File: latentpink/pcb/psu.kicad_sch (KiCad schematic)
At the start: 0 parts

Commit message: Continued initial schematic capture and floorplanning
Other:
- company: (none) -> Antikernel Labs
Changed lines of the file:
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@@
 (kicad_sch (version 20211123) (generator eeschema)
   (paper "A4")
+  (title_block
+    (date "2023-04-22")
+    (rev "0.1")
+    (company "Antikernel Labs")
+    (comment 1 "Andrew D. Zonenberg")
+  )
 )

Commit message: Continued initial schematic capture
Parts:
- added C100, C101, C102, C103, C104, C105, C89, C90, C94, C95: 22 uF 25V, symbol device:C
- added C106: 4.7 uF, azonenberg_pcb:EIA_0603_CAP_NOSILK, symbol device:C
- added C107, C108, C109, C112, C113, C114, C91, C92, C93, C96, C97: 220 uF, symbol device:C
- added C110, C115, C116, C119, C123: 0.47 uF, azonenberg_pcb:EIA_0402_CAP_NOSILK, symbol device:C
- added C111: 0.1 uF, azonenberg_pcb:EIA_0402_CAP_NOSILK, symbol device:C
- added C117, C122: EEH-ZS1E102UV, symbol device:CP1
- added C118, C120: DNP, symbol device:CP1
- added C121: 0.015 uF, azonenberg_pcb:EIA_0603_CAP_NOSILK, symbol device:C
- added D1, D2, D3: GREEN, azonenberg_pcb:EIA_0603_LED, symbol device:LED
- added D4: RED, azonenberg_pcb:EIA_0603_LED, symbol device:LED
- added F1: 4A, symbol power-azonenberg:FUSE_PWROUT_2
- added FB1: TBD, symbol passive-azonenberg:FERRITE_SMALL2
- added J13: CONN_01X05, azonenberg_pcb:CONN_HEADER_2.54MM_1x5, symbol conn:CONN_01X05
- added J14: CONN_01X03, azonenberg_pcb:CONN_HEADER_2.54MM_1x3, symbol conn:CONN_01X03
- added J6: BARREL_JACK, azonenberg_pcb:CONN_CUI_PJ-058BH_HIPWR_BARREL_NOSLOT, symbol power-azonenberg:BARREL_JACK
- added R1: 16K, symbol device:R
- added R10: 4.7k, azonenberg_pcb:EIA_0402_RES_NOSILK, symbol device:R
- added R11: 160, symbol device:R
- added R12: 22, symbol device:R
- added R13: 300, symbol device:R
- added R14, R16, R18, R20, R22, R5, R7: 10K, azonenberg_pcb:EIA_0402_RES_NOSILK, symbol device:R
- added R15, R17, R19, R21, R23, R29, R31: 1K, azonenberg_pcb:EIA_0402_RES_NOSILK, symbol device:R
- added R2, R6: 0, azonenberg_pcb:EIA_0402_RES_NOSILK, symbol device:R
- added R24, R25, R26, R27: 470, azonenberg_pcb:EIA_0402_RES_NOSILK, symbol device:R
- added R28: 470 1/4W, symbol device:R
- added R8: 3k, symbol device:R
- added R9: 2.2k, symbol device:R
- added TP1, TP2, TP3, TP4, TP5: TESTPOINT, azonenberg_pcb:TESTPOINT_SMT_0.5MM, symbol conn:CONN_01X01
- added U10: MYMGK1R812ERSR, azonenberg_pcb:MODULE_MURATA_MYMGK1R812, symbol power-azonenberg:MYMGK1R812ERSR
- added U11, U13, U14, U15: MYMGK00504ERSR, azonenberg_pcb:MODULE_MURATA_MYMGK00504ERSR, symbol power-azonenberg:MYMGK00504ERSR
- added U12: STM32L031-QFN32, azonenberg_pcb:QFN_32_0.5MM_5x5MM, symbol st-azonenberg:STM32L031-QFN32
- added U16, U17: NCP45521IMNTWG-H, azonenberg_pcb:DFN_8_0.5MM_2x2MM, symbol power-azonenberg:NCP45525
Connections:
- new net: D3.2 (A), R26.2
- new net: C121.1, U16.6 (SR)
- new net: R10.2, R13.2
- new net: R8.1, U13.4 (TRIM)
- new net: R11.2, R8.2
- new net: D4.2 (A), R27.2
- new net: R5.2, R6.2
- new net: R9.1, U14.4 (TRIM)
- new net: R12.2, R9.2
- new net: R10.1, U15.4 (TRIM)
- new net: R1.2, R2.2
- new net: R5.1, U11.4 (TRIM)
- new net: R1.1, U10.22 (TRIM)
- new net: D1.2 (A), R24.2
- new net: F1.2, FB1.1
- new net: D2.2 (A), R25.2
- new net 12V0: C100.1, C101.1, C102.1, C103.1, C104.1, C105.1, C117.1, C118.1, C120.1, C122.1, C89.1, C90.1, C94.1, C95.1, R28.2, U10.1 (VIN), U10.2 (VIN), U10.3 (VIN), U10.4 (VIN), U10.5 (VIN), U10.6 (VIN), U11.1 (VIN), U11.2 (VIN), U13.1 (VIN), U13.2 (VIN), U14.1 (VIN), U14.2 (VIN), U15.1 (VIN), U15.2 (VIN), U16.7 (VOUT), U16.8 (VOUT)
- new net 12V0_BLEED: R28.1, U16.5 (BLEED)
- new net 12V0_EN: R29.1, U12.22 (PA12), U16.2 (EN)
- new net 12V0_FUSED: FB1.2, U16.1 (VIN), U16.PAD (VIN)
- new net 12V0_RAW: F1.1, J6.1 (PWR)
- new net 1V0: C91.1, C92.1, C93.1, U10.15 (VOUT), U10.16 (VOUT), U10.17 (VOUT), U10.18 (VOUT), U10.19 (VOUT), U10.20 (VOUT), U10.21 (SENSE)
- new net 1V0_EN: R15.1, U10.8 (EN), U12.19 (PA9)
- new net 1V0_PGOOD: R14.1, TP2.1 (P1), U10.7 (PGOOD), U12.6 (PA0)
- new net 1V2: C96.1, C97.1, U11.5 (SENSE), U11.6 (VOUT), U11.7 (VOUT)
- new net 1V2_EN: R17.1, U11.12 (ON/OFF), U12.18 (PA8)
- new net 1V2_PGOOD: R16.1, TP1.1 (P1), U11.11 (PGOOD), U12.7 (PA1)
- new net 1V8: C109.1, C114.1, U15.5 (SENSE), U15.6 (VOUT), U15.7 (VOUT), U17.1 (VIN), U17.PAD (VIN)
- new net 1V8_EN: R19.1, U12.13 (PA7), U15.12 (ON/OFF)
- new net 1V8_IO: U17.5 (BLEED), U17.7 (VOUT), U17.8 (VOUT)
- new net 1V8_IO_EN: R31.1, U12.25 (PA15), U17.2 (EN)
- new net 1V8_PGOOD: R18.1, TP5.1 (P1), U12.8 (PA2), U15.11 (PGOOD)
- new net 2V5: C107.1, C112.1, U13.5 (SENSE), U13.6 (VOUT), U13.7 (VOUT)
- new net 2V5_EN: R21.1, U12.12 (PA6), U13.12 (ON/OFF)
- new net 2V5_PGOOD: R20.1, TP3.1 (P1), U12.9 (PA3), U13.11 (PGOOD)
- new net 3V3: C108.1, C113.1, U14.5 (SENSE), U14.6 (VOUT), U14.7 (VOUT)
- new net 3V3_EN: R23.1, U12.11 (PA5), U14.12 (ON/OFF)
- new net 3V3_PGOOD: R22.1, TP4.1 (P1), U12.10 (PA4), U14.11 (PGOOD)
- new net 3V3_SB: C106.1, C110.1, C115.1, C116.1, C119.1, C123.1, J13.1 (P1), R14.2, R16.2, R18.2, R20.2, R22.2, R25.1, U12.1 (VDD), U12.17 (VDD), U12.5 (VDDA), U16.3 (VCC), U17.3 (VCC)
- new net ALL_OK: R24.1, U12.32 (PB8)
- new net FPGA_DONE: U12.16 (PB2)
- new net FPGA_INIT: U12.26 (PB3)
- new net FPGA_RST_N: U12.15 (PB1)
- new net GND: C100.2, C101.2, C102.2, C103.2, C104.2, C105.2, C106.2, C107.2, C108.2, C109.2, C110.2, C111.2, C112.2, C113.2, C114.2, C115.2, C116.2, C117.2, C118.2, C119.2, C120.2, C121.2, C122.2, C123.2, C89.2, C90.2, C91.2, C92.2, C93.2, C94.2, C95.2, C96.2, C97.2, D1.1 (K), D2.1 (K), D3.1 (K), D4.1 (K), J13.2 (P2), J14.3 (P3), J6.2 (GND), R11.1, R12.1, R13.1, R15.2, R17.2, R19.2, R2.1, R21.2, R23.2, R29.2, R31.2, R6.1, R7.2, U10.10 (GND), U10.11 (GND), U10.12 (GND), U10.13 (GND), U10.14 (GND), U10.23 (GND), U10.24 (GND), U10.25 (GND), U10.26 (GND), U10.27 (GND), U10.28 (GND), U10.29 (GND), U10.30 (GND), U10.31 (GND), U10.32 (GND), U10.33 (GND), U10.34 (GND), U10.35 (GND), U10.36 (GND), U10.37 (GND), U10.9 (GND), U11.10 (GND), U11.13 (GND), U11.14 (GND), U11.15 (GND), U11.16 (GND), U11.17 (GND), U11.18 (GND), U11.19 (GND), U11.20 (GND), U11.21 (GND), U11.22 (GND), U11.23 (GND), U11.3 (GND), U11.8 (GND), U11.9 (GND), U12.PAD (GND), U13.10 (GND), U13.13 (GND), U13.14 (GND), U13.15 (GND), U13.16 (GND), U13.17 (GND), U13.18 (GND), U13.19 (GND), U13.20 (GND), U13.21 (GND), U13.22 (GND), U13.23 (GND), U13.3 (GND), U13.8 (GND), U13.9 (GND), U14.10 (GND), U14.13 (GND), U14.14 (GND), U14.15 (GND), U14.16 (GND), U14.17 (GND), U14.18 (GND), U14.19 (GND), U14.20 (GND), U14.21 (GND), U14.22 (GND), U14.23 (GND), U14.3 (GND), U14.8 (GND), U14.9 (GND), U15.10 (GND), U15.13 (GND), U15.14 (GND), U15.15 (GND), U15.16 (GND), U15.17 (GND), U15.18 (GND), U15.19 (GND), U15.20 (GND), U15.21 (GND), U15.22 (GND), U15.23 (GND), U15.3 (GND), U15.8 (GND), U15.9 (GND), U16.4 (GND), U17.4 (GND)
- new net HARD_RESET_REQ: U12.28 (PB5)
- new net MCU_HEARTBEAT: U12.27 (PB4)
- new net MCU_RST_N: U12.14 (PB0)
- new net PWR_FAIL: R27.1, U12.21 (PA11)
- new net PWR_OK: R26.1, U12.20 (PA10)
- new net SUPER_BOOT0: R7.1, U12.31 (BOOT0)
- new net SUPER_RST_N: C111.1, J13.5 (P5), U12.4 (NRST)
- new net SUPER_SWCLK: J13.3 (P3), U12.24 (PA14)
- new net SUPER_SWDIO: J13.4 (P4), U12.23 (PA13)
- new net SUPER_UART_RX: J14.1 (P1), U12.30 (PB7)
- new net SUPER_UART_TX: J14.2 (P2), U12.29 (PB6)
- no-connect marks 0 -> 4
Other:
- note added: "1.5V Vih, 1.1V Vil Internal: 6.8k pulldown, 22k pullup So should float at ~2.8V if undriven Add external 1K pulldown, equivalent 871 ohms Need 1.72 mA drive current for 1.5V, 2.87 mA for 2.5V"
- note added: "1.8V Vih Internal: 33K pulldown, 100K pullup So should float at ~2.7V if undriven"
- note added: "115 ohm nominal internal bleed resistance Max 400 mW internal dissipation 470 will gives discharge current of 20.5 mA Resistor will dissipate ~200 mW, 48 mW in IC"
- note added: "Cmax = 7.8A / SR SR for 3.3V supply = 13.5 kV/s Max C with default slew is only 578 uF To support 3000 uF (allowing for extra C), we need slew of 2.6 kV/sec or less SR = 31 uA / Csr so Csr = 11.9 nF"
- note added: "Power rail sequencing requirements: * QDR: VDD before VDDQ, VDDQ before or simultaneous w/ Vref * FPGA: 1V0 -> 1V8 -> VCCO * FPGA: 1V0 -> 1V2 Overall sequence: * Vin * 3V3_SB * 12V0 * 1V0 * 1V2 / 1V8 simultaneous * 1V8_IO, 2V5, 3V3 simultaneous * FPGA reset * MCU reset"
- note added: "Total output C 400 - 3000 uF"
- note added: "Total output C 660 - 5000 uF"
- note added: "Trim: Precision metal film 1/10W +/- 0.5%"

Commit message: Continued work on schematic, mostly power supply and QDR
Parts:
- added C167, C168: 0.1 uF, azonenberg_pcb:EIA_0402_CAP_NOSILK, symbol device:C
- added C169: 22 uF, symbol device:C
- added C170, C172: 0.47 uF, azonenberg_pcb:EIA_0402_CAP_NOSILK, symbol device:C
- added C171: 220 uF, symbol device:C
- added C173, C174: 2.2 uF, symbol device:C
- added R32: 1K, azonenberg_pcb:EIA_0402_RES_NOSILK, symbol device:R
- added R33, R34, R35, R36, R37, R38: 0, azonenberg_pcb:EIA_0402_RES_NOSILK, symbol device:R
- added R39: R, symbol device:R
- added TP16: TESTPOINT, azonenberg_pcb:TESTPOINT_SMT_0.5MM, symbol conn:CONN_01X01
- added U18: LP2996AMRE, azonenberg_pcb:SOIC_8_3.9MM_EPAD, symbol power-azonenberg:LP2996A
- added U19: TPS7A2533DRVR, symbol power-azonenberg:TPS7A25
- F1: value 4A -> ERB-RD4R00X; footprint (none) -> azonenberg_pcb:EIA_0402_CAP_NOSILK
- FB1: value TBD -> BLM31KN271SN1L; footprint (none) -> azonenberg_pcb:EIA_1206_CAP_NOSILK
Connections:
- net 12V0_FUSED: now also C174.1, U19.4 (EN), U19.6 (IN)
- net 1V0: now also R33.2, R35.2; no longer C91.1, C92.1, C93.1, U10.15 (VOUT), U10.16 (VOUT), U10.17 (VOUT), U10.18 (VOUT), U10.19 (VOUT), U10.20 (VOUT), U10.21 (SENSE)
- net 1V2: now also R34.2; no longer C96.1, C97.1, U11.6 (VOUT), U11.7 (VOUT)
- net 1V8: now also C169.1, C170.1, R38.2, U18.5 (VDDQ), U18.7 (PVIN); no longer C109.1, C114.1, U15.6 (VOUT), U15.7 (VOUT)
- net 2V5: now also R36.2; no longer C107.1, C112.1, U13.6 (VOUT), U13.7 (VOUT)
- net 3V3: now also C172.1, R37.2, U18.6 (AVIN); no longer C108.1, C113.1, U14.6 (VOUT), U14.7 (VOUT)
- net 3V3_SB: now also C173.1, R39.2, U19.1 (OUT)
- net GND: now also C167.2, C168.2, C169.2, C170.2, C171.2, C172.2, C173.2, C174.2, R32.2, U18.1 (GND), U18.PAD (GND), U19.5 (GND), U19.PAD (GND)
- net VTT_EN: now reaches U12.2 (PC14)
- net VTT_EN: now also R32.1, U18.2 (~{SD})
- new net 1V0_RAW: C91.1, C92.1, C93.1, R33.1, U10.15 (VOUT), U10.16 (VOUT), U10.17 (VOUT), U10.18 (VOUT), U10.19 (VOUT), U10.20 (VOUT)
- new net 1V0_SENSE: R35.1, U10.21 (SENSE)
- new net 1V2_RAW: C96.1, C97.1, R34.1, U11.6 (VOUT), U11.7 (VOUT)
- new net 1V8_RAW: C109.1, C114.1, R38.1, U15.6 (VOUT), U15.7 (VOUT)
- new net 2V5_RAW: C107.1, C112.1, R36.1, U13.6 (VOUT), U13.7 (VOUT)
- new net 3V3_RAW: C108.1, C113.1, R37.1, U14.6 (VOUT), U14.7 (VOUT)
- new net 3V3_SB_PGOOD: R39.1, TP16.1 (P1), U19.3 (PG)
- new net QDR_VREF: C167.1, U18.4 (VREF)
- new net QDR_VTT: C168.1, C171.1, U18.3 (VSENSE), U18.8 (VTT)
- no-connect marks 4 -> 3
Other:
- note added: "Place C168 near U18 pin 3"
- note added: "Place C169 by U18 pin 7 Place C170 by U18 pin 5"
- note added: "Slew rate 2.1 kV/sec, so 5.7 ms ramp time Estimated 6.3A peak inrush"
- note added: "TODO: FPGA_RST_N / FPGA_DONE / FPGA_INIT are LVCMOS18 Do we need level shifting? We can do open drain on outputs So should only be an issue for DONE input"
- moved on the sheet: C119, C121, D1, D2, D3, D4, R14, R15, R16, R17, R18, R19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

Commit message: Continued work on QSGMII subsystem
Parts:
- R28: footprint (none) -> azonenberg_pcb:EIA_0603_RES_NOSILK
- U19: footprint (none) -> azonenberg_pcb:DFN_6_0.65MM_2x2MM
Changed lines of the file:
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@@
   (paper "A3")
   (title_block
-    (date "2023-05-10")
+    (date "2023-05-14")
     (rev "0.1")
     (company "Antikernel Labs")
@@
     (property "Reference" "U19" (id 0) (at 337.185 71.281 0))
     (property "Value" "TPS7A2533DRVR" (id 1) (at 337.185 73.8179 0))
-    (property "Footprint" "" (id 2) (at 331.47 83.82 0)
+    (property "Footprint" "azonenberg_pcb:DFN_6_0.65MM_2x2MM" (id 2) (at 331.47 83.82 0)
       (effects (font (size 1.27 1.27)) hide)
     )
@@
     (property "Reference" "R28" (id 0) (at 194.31 24.13 90))
     (property "Value" "470 1/4W" (id 1) (at 187.96 26.67 90))
-    (property "Footprint" "" (id 2) (at 187.96 25.908 90)
-      (effects (font (size 1.27 1.27)) hide)
-    )
+    (property "Footprint" "azonenberg_pcb:EIA_0603_RES_NOSILK" (id 2) (at 187.96 25.908 90)
+      (effects (font (size 1.27 1.27)) hide)
+    )

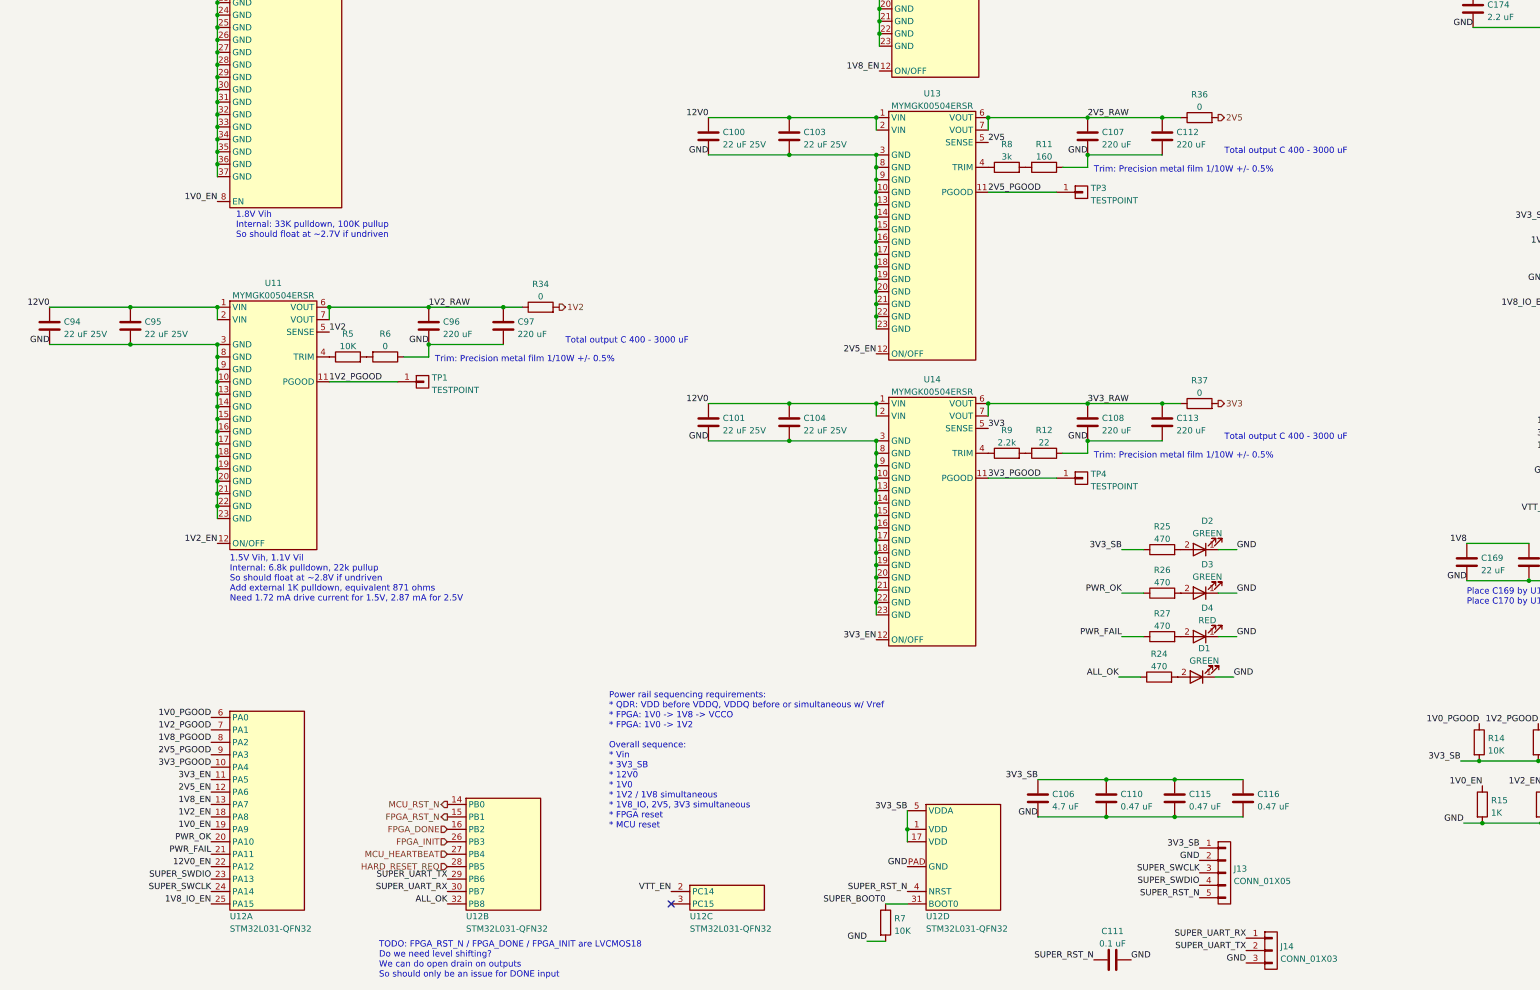
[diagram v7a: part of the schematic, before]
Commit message: Continued footprint assignment and miscellaneous missing tidbits of schematic
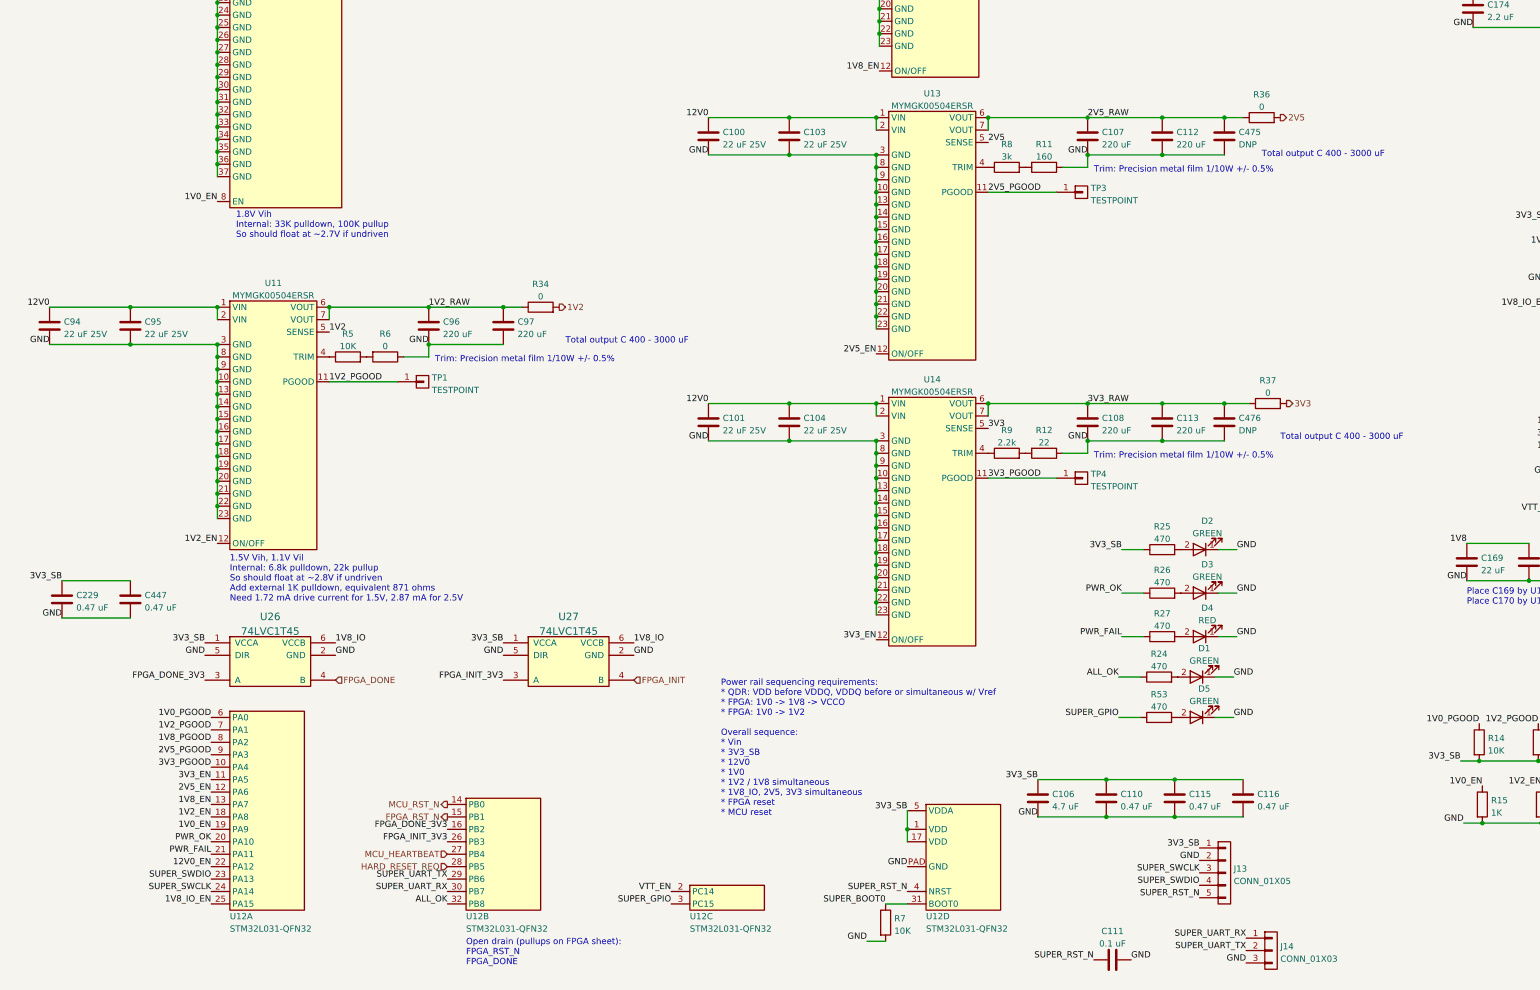
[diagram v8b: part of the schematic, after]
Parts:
- added C229, C447: 0.47 uF, azonenberg_pcb:EIA_0402_CAP_NOSILK, symbol device:C
- added C475, C476: DNP, azonenberg_pcb:EIA_1210_CAP_NOSILK, symbol device:C
- added D5: GREEN, azonenberg_pcb:EIA_0603_LED, symbol device:LED
- added R53: 470, azonenberg_pcb:EIA_0402_RES_NOSILK, symbol device:R
- added U26, U27: 74LVC1T45, azonenberg_pcb:DFN_6_0.5MM_1.45x1.00MM, symbol special-azonenberg:74LVC1T45
- C100, C101, C102, C103, C104, C105, C89, C90, C94, C95: footprint (none) -> azonenberg_pcb:EIA_1812_CAP_NOSILK
- C107, C108, C109, C112, C113, C114, C91, C92, C93, C96, C97: footprint (none) -> azonenberg_pcb:EIA_1210_CAP_NOSILK
- C117, C118, C120, C122: footprint (none) -> azonenberg_pcb:CAP_AL_10MM_SMT
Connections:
- net 1V8_IO: now also U26.6 (VCCB), U27.6 (VCCB)
- net 2V5_RAW: now also C475.1
- net 3V3_RAW: now also C476.1
- net 3V3_SB: now also C229.1, C447.1, U26.1 (VCCA), U27.1 (VCCA)
- net FPGA_DONE: now also U26.4 (B); no longer U12.16 (PB2)
- net FPGA_INIT: now also U27.4 (B); no longer U12.26 (PB3)
- net GND: now also C229.2, C447.2, C475.2, C476.2, D5.1 (K), U26.2 (GND), U26.5 (DIR), U27.2 (GND), U27.5 (DIR)
- net SUPER_GPIO: now reaches U12.3 (PC15)
- net SUPER_GPIO: now also R53.1
- new net: D5.2 (A), R53.2
- new net FPGA_DONE_3V3: U12.16 (PB2), U26.3 (A)
- new net FPGA_INIT_3V3: U12.26 (PB3), U27.3 (A)
- no-connect marks 3 -> 2
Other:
- note added: "Open drain (pullups on FPGA sheet): FPGA_RST_N FPGA_DONE"
- note removed: "TODO: FPGA_RST_N / FPGA_DONE / FPGA_INIT are LVCMOS18 Do we need level shifting? We can do open drain on outputs So should only be an issue for DONE input"
- moved on the sheet: R36, R37
